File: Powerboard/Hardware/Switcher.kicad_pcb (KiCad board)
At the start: 4 copper layers, 47 x 50 mm, 118 parts, among them IC2 SiC437BED-T1-GE3, J1 Conn_01x03_MountingPin, J2 XT60PW-F, J3 USB_C_Receptacle_USB2.0, J4 Conn_01x02_Male, J5 Conn_01x08_Male, J6 Conn_01x02_Male, J7 XT60PW-M, J8 Conn_01x04_Male, Q1 PXP012-30QLJ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

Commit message: new layout
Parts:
- removed J2: XT60PW-F, iclr:AMASS_XT60PW-F
- added J9: XT60PW-M, iclr:AMASS_XT60PW-M, F.Cu at (111.6, 24.6)
- JP2, JP3, R14, R18, R19, R22, R24, R26: moved to F.Cu
- moved J8 45.7 mm to (68.3, 36.2)
- moved J6 42.9 mm to (68.4, 60.6), turned to 0 degrees
- moved R19 40.4 mm to (71.5, 63.0), turned to 90 degrees
- moved R22 40.3 mm to (121.5, 30.7), turned to 0 degrees
- moved JP3 38.7 mm to (71.4, 60.4), turned to 90 degrees
- moved R14 38.3 mm to (120.5, 29.8), turned to 0 degrees
- moved 3V3LED1 38.2 mm to (121.4, 38.2), turned to 180 degrees
- moved R7 36.3 mm to (120.4, 37.2), turned to 180 degrees
- moved 12VLED1 33.7 mm to (121.5, 33.1), turned to 180 degrees
- moved R9 31.7 mm to (120.5, 32.2), turned to 0 degrees
- moved C53 23.8 mm to (90.1, 42.1), turned to 180 degrees
- moved J7 23.0 mm to (95.6, 24.6), turned to 0 degrees
- moved C54 22.4 mm to (90.1, 43.0), turned to 180 degrees
- moved Q5 21.4 mm to (109.7, 35.3)
- moved U1 21.2 mm to (110.5, 39.6)
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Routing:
- net /SDA: track 53.7 -> 5.53 mm
- net /SCL: track 51.8 -> 5.68 mm
- net /DeploymentVoltage: track 19.5 -> 60.7 mm, vias 1 -> 2
- net /12V_SWITCH: track 50.4 -> 22.0 mm, vias 1 -> 0
- net Net-(J4-Pin_1): track 16.1 -> 41.0 mm, vias 1 -> 2
- net /LIPOPOWER: track 22.5 -> 42.5 mm
- net /PDU_EN: track 29.4 -> 13.4 mm
- net /3V3LOG: track 13.6 -> 28.5 mm, vias 1 -> 0
- net Net-(J6-Pin_1): track 36.0 -> 50.2 mm, vias 1 -> 2
- net +12V: track 21.0 -> 8.61 mm, vias 20 -> 18
- net /CAN_TX: track 14.0 -> 25.1 mm
- net /CAN_RX: track 8.54 -> 18.6 mm
- net Net-(J5-Pin_4): track 0.00 -> 9.77 mm, vias 9 -> 0
- net /USBPOWER: track 18.9 -> 27.0 mm
- net Net-(U2-U0RXD/PROG/GPIO44): track 11.1 -> 4.00 mm
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- added copper zone on F.Cu, net /3V3Filter/FBIn
- added copper zone on B.Cu, net /3V3Filter/LX1
- added copper zone on F.Cu, net /3V3Filter/LX1
- added copper zone on B.Cu, net /3V3Filter/LX2
- added copper zone on F.Cu, net /3V3Filter/LX2
- removed copper zone on B.Cu, net Net-(J5-Pin_4)
- removed copper zone on B.Cu, net Net-(Q1-S_1)
- removed copper zone on B.Cu, net RBUS_uC_V
- removed copper zone on B.Cu, net VBUS
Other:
- board size 47 x 50 mm -> 60 x 50 mm
- board text added: "12V LED"
- board text added: "12V SWITCH"
- board text added: "3V3 LED"
- board text added: "3V3 SWITCH"
- board text added: "ARMING"
- board text added: "D+"
- board text added: "D-"
- board text added: "VBUS LED"
- board text removed: "+"
- board text removed: "12V"
- board text removed: "3V3"
- board text removed: "3V3_SWITCH"
- board text removed: "D"
- board text removed: "PDU_EN"

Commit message: silkscreen
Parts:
- moved locked 4.14 mm to (103.2, 49.5)
- moved G*** 2.19 mm to (79.9, 36.7)
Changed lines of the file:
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@@
   )
   (footprint "iclr:LMQ" (layer "B.Cu")
-    (at 99.124934 49.894145 180)
+    (at 103.244934 49.474145 180)
     (attr board_only exclude_from_pos_files exclude_from_bom)
     (fp_text reference locked "G***" (at -1.676 0.436 unlocked) (layer "B.Fab")
@@
   )
   (footprint "iclr:kachow" (layer "B.Cu")
-    (at 77.82 37.37 180)
+    (at 79.9 36.7 180)
     (attr board_only exclude_from_pos_files exclude_from_bom)
     (fp_text reference "G***" (at -1.47 -0.01 unlocked) (layer "B.Fab")
@@
     (effects (font (size 0.65 0.65) (thickness 0.15)) (justify mirror))
   )
-  (gr_text "Lightning McQueen v2.0" (at 96.2 36.39) (layer "B.SilkS")
+  (gr_text "Lightning McQueen v2.0" (at 102.2 36.5) (layer "B.SilkS")
     (effects (font (size 1.2 1.2) (thickness 0.3)) (justify mirror))
   )
@@
     (effects (font (size 0.7 0.7) (thickness 0.15) bold) (justify left bottom))
   )
-  (gr_text "ISOL" (at 105.86 30.46) (layer "F.SilkS")
-    (effects (font (size 0.7 0.7) (thickness 0.15) bold) (justify left bottom))
-  )

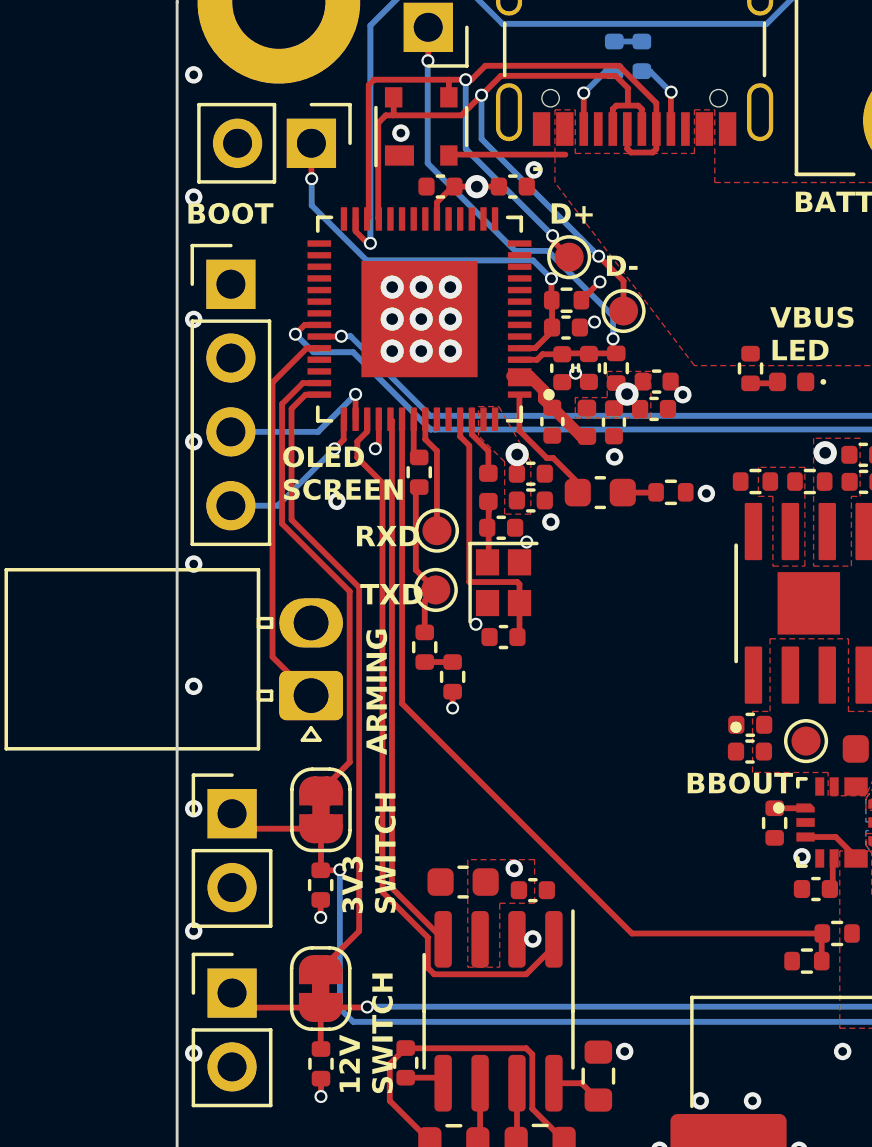
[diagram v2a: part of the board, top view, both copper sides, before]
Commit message: fixed cap in wrong place
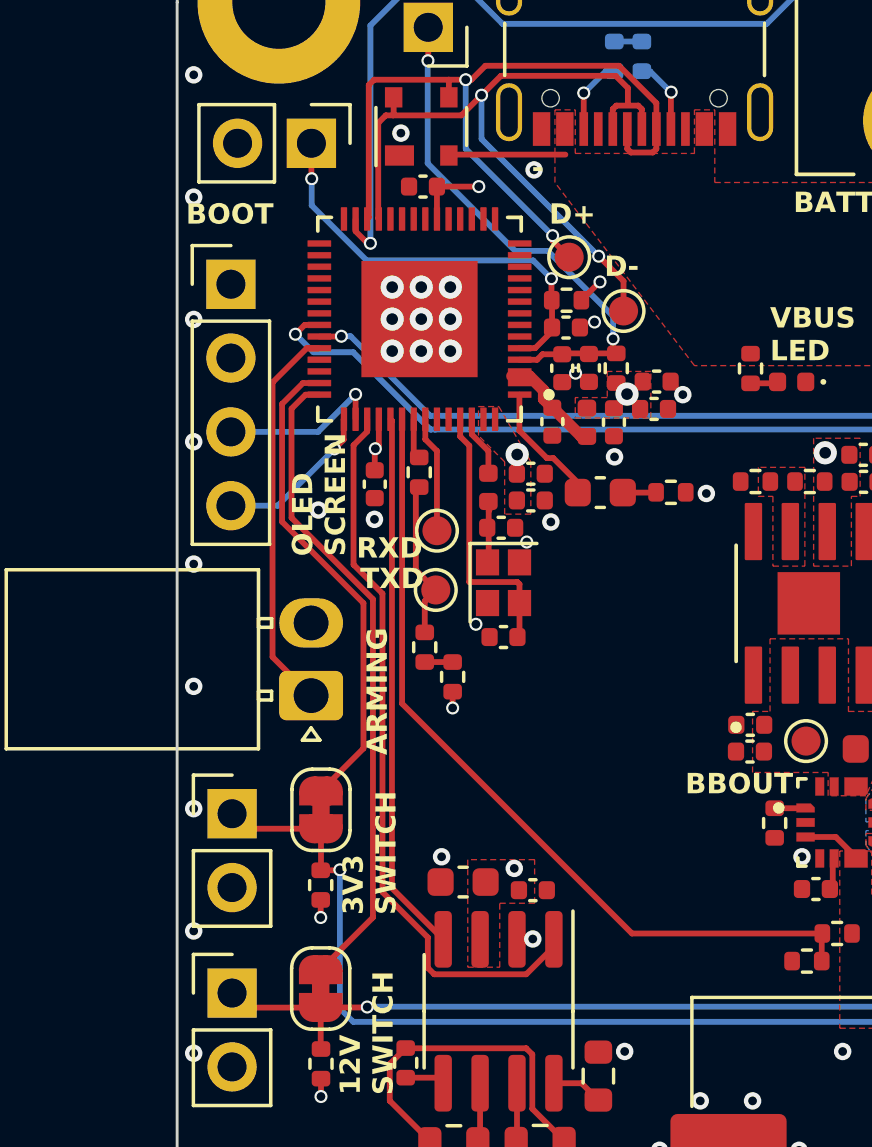
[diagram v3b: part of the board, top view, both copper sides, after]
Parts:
- moved C10 11.3 mm to (73.3, 43.1), turned to -90 degrees
- moved C11 0.60 mm to (75.0, 32.8)
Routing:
- net GND: vias 103 -> 105

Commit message: changes
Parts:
- C19: footprint Capacitor_SMD:C_0603_1608Metric -> Capacitor_SMD:C_0402_1005Metric
- moved R5 4.91 mm to (79.2, 53.4)
- moved TXLED1 4.90 mm to (78.2, 52.4)
- moved TP5 4.70 mm to (78.3, 48.4)
- moved TP4 4.70 mm to (78.2, 50.5)
- moved C13 3.70 mm to (75.7, 45.2), turned to 90 degrees
- moved R4 2.01 mm to (73.6, 44.3)
- moved C14 1.98 mm to (79.5, 45.4), turned to -90 degrees
- moved Y1 1.30 mm to (77.6, 45.2), turned to 180 degrees
- moved R17 0.95 mm to (76.8, 66.2)
- moved R23 0.95 mm to (75.2, 63.5)
- moved U5 0.95 mm to (78.4, 61.7)
- moved C20 0.95 mm to (80.8, 67.8)
- moved D2 0.95 mm to (78.3, 68.8)
- moved R15 0.95 mm to (81.8, 64.0)
- moved R16 0.95 mm to (79.8, 66.2)
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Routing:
- net Net-(U2-U0RXD/PROG/GPIO44): track 4.00 -> 10.6 mm
- net RBUS_uC_V: track 12.7 -> 18.8 mm
- net /TXD: track 5.49 -> 9.07 mm
- net Net-(U2-XTAL_N): track 9.34 -> 7.26 mm
- net /CAN_TX: track 25.2 -> 23.2 mm, vias 0 -> 2
- net Net-(U2-U0TXD/PROG/GPIO43): track 1.39 -> 3.35 mm
- net /3V3LOG: track 28.5 -> 30.4 mm, vias 0 -> 2
- net /CAN_RX: track 18.6 -> 20.3 mm, vias 0 -> 2
- net /CAN+: track 43.8 -> 42.6 mm
- net /CAN-: track 45.2 -> 44.1 mm
- net GND: track 4.02 -> 4.99 mm, vias 105 -> 115
- net Net-(C14-Pad1): track 2.11 -> 2.97 mm
- net /LIPOPOWER: track 42.5 -> 41.9 mm
- net +12V: track 8.61 -> 8.85 mm, vias 18 -> 45
- net Net-(J7-+): vias 0 -> 16
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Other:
- board text removed: "12V_SWITCH"

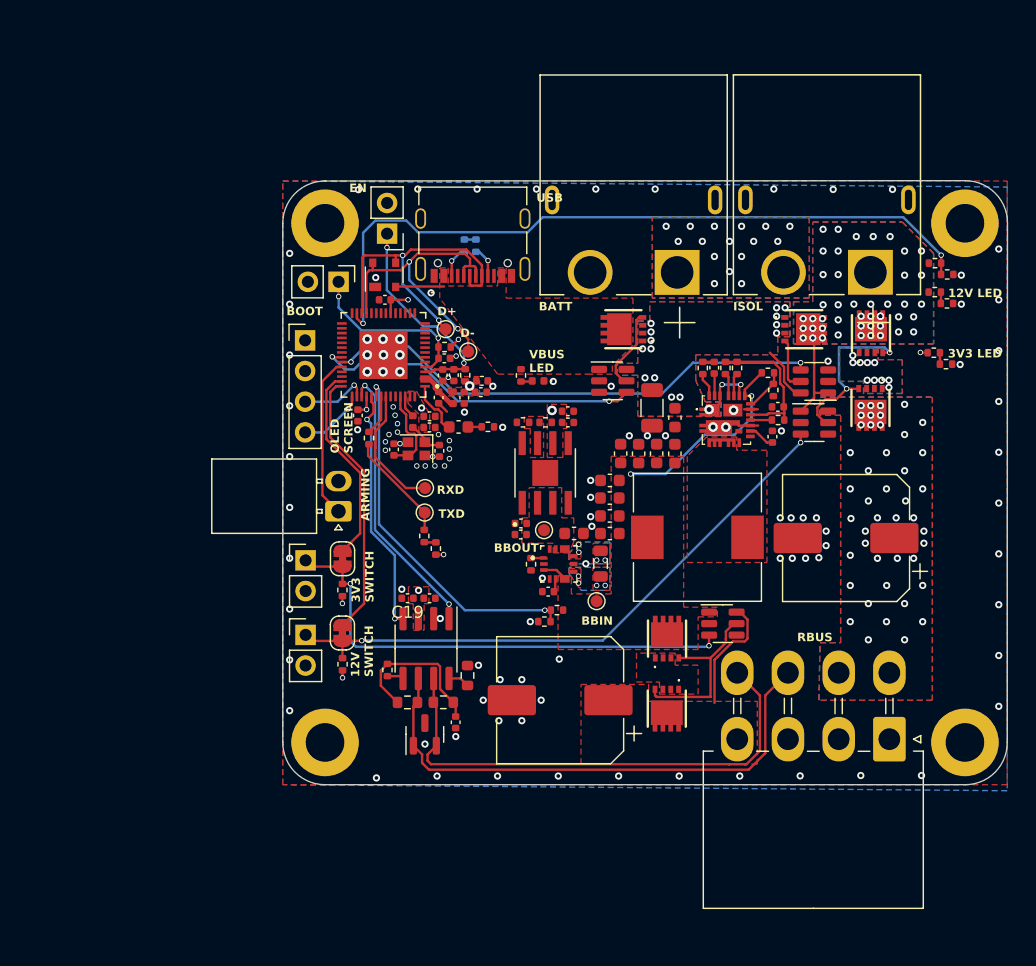
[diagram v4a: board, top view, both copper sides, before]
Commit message: new inductor, logging traces rerouted
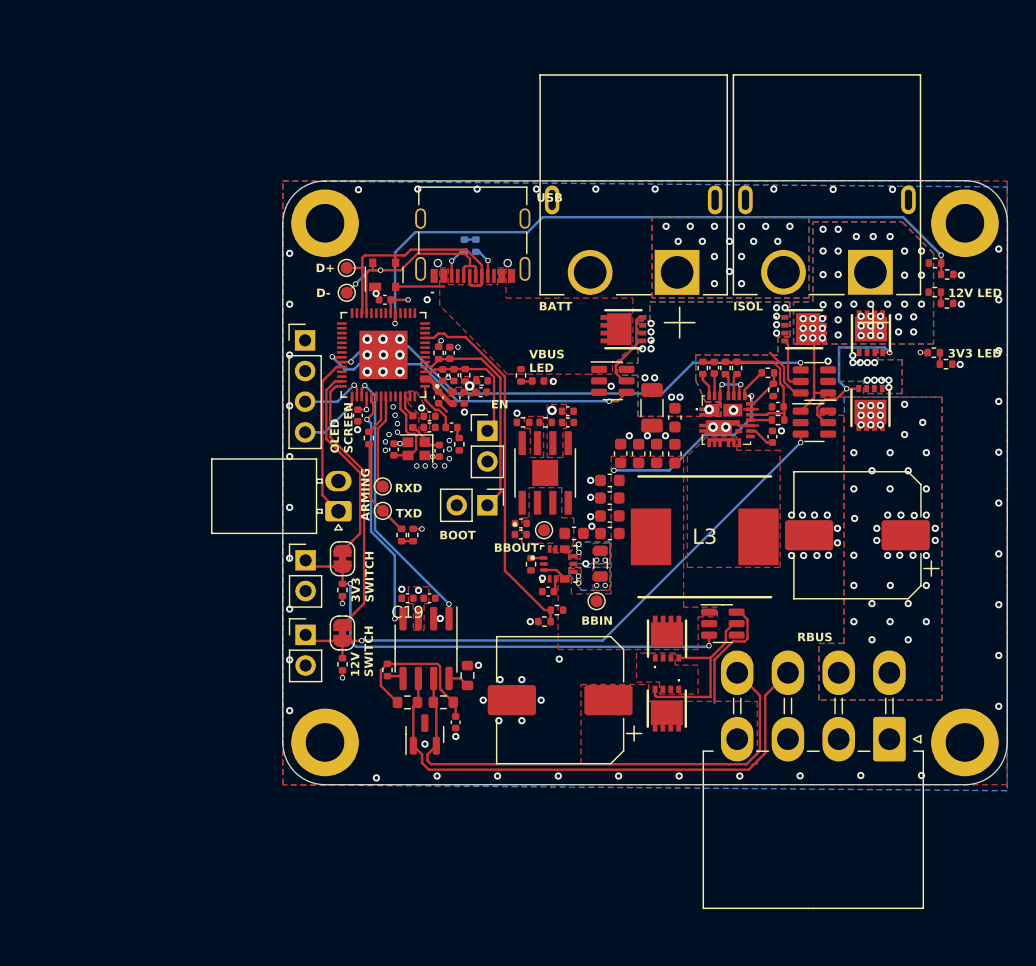
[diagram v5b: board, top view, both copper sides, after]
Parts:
- removed L4: 3.3uH, Inductor_SMD:L_10.4x10.4_H4.8
- added L3: SRP1050WA-3R3M, iclr:INDPM110100X540N, F.Cu at (101.5, 52.5)
- C12: value 4.2pF -> DNP; footprint Capacitor_SMD:C_0603_1608Metric -> Capacitor_SMD:C_0402_1005Metric
- R8: value 47.5 -> DNP
- moved BOOTJUMPER1 22.2 mm to (83.4, 49.9)
- moved ENJUMPER1 18.3 mm to (83.5, 43.7), turned to 0 degrees
- moved TP2 11.2 mm to (71.8, 32.3)
- moved TP1 9.64 mm to (71.8, 30.2)
- moved TP5 3.50 mm to (74.8, 48.3)
- moved TP4 3.46 mm to (74.8, 50.3)
- moved R8 2.77 mm to (81.1, 44.8), turned to 90 degrees
- moved R5 2.19 mm to (77.3, 52.3), turned to -90 degrees
- moved TXLED1 1.87 mm to (76.3, 52.3)
- moved C24 0.97 mm to (114.1, 52.3)
- moved R6 0.69 mm to (79.4, 37.2), turned to -90 degrees
- moved C8 0.64 mm to (80.3, 37.2), turned to 90 degrees
- moved C12 0.58 mm to (80.5, 43.4)
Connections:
- U2 pad 11: unconnected-(U2-GPIO6/ADC1_CH5-Pad11) -> /3V3LOG
- U2 pad 19: unconnected-(U2-GPIO14/ADC2_CH3-Pad19) -> /DeploymentVoltage
- U2 pad 27: /DeploymentVoltage -> unconnected-(U2-GPIO21-Pad27)
- U2 pad 48: /3V3LOG -> unconnected-(U2-MTMS/JTAG/GPIO42-Pad48)
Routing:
- net /CHIP_PU: track 18.0 -> 10.8 mm, vias 2 -> 0
- net /Data+: track 26.9 -> 20.6 mm, vias 2 -> 0
- net /Data-: track 25.8 -> 20.0 mm
- net /DeploymentVoltage: track 60.7 -> 56.1 mm
- net /BOOT: track 14.6 -> 18.2 mm, vias 2 -> 0
- net Net-(U2-U0RXD/PROG/GPIO44): track 10.6 -> 7.90 mm
- net RBUS_uC_V: track 18.8 -> 20.1 mm
- net /TXD: track 9.07 -> 8.17 mm
- net /3V3LOG: vias 2 -> 0
- net GND: vias 115 -> 113
- net +12V: vias 45 -> 44
